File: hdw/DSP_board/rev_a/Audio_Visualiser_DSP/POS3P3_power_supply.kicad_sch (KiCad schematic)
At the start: 25 parts, among them Q401 BSS214NW, Q402 ZXMS6004FFTA, U401 74LVC1G97, U402 TPS62130A

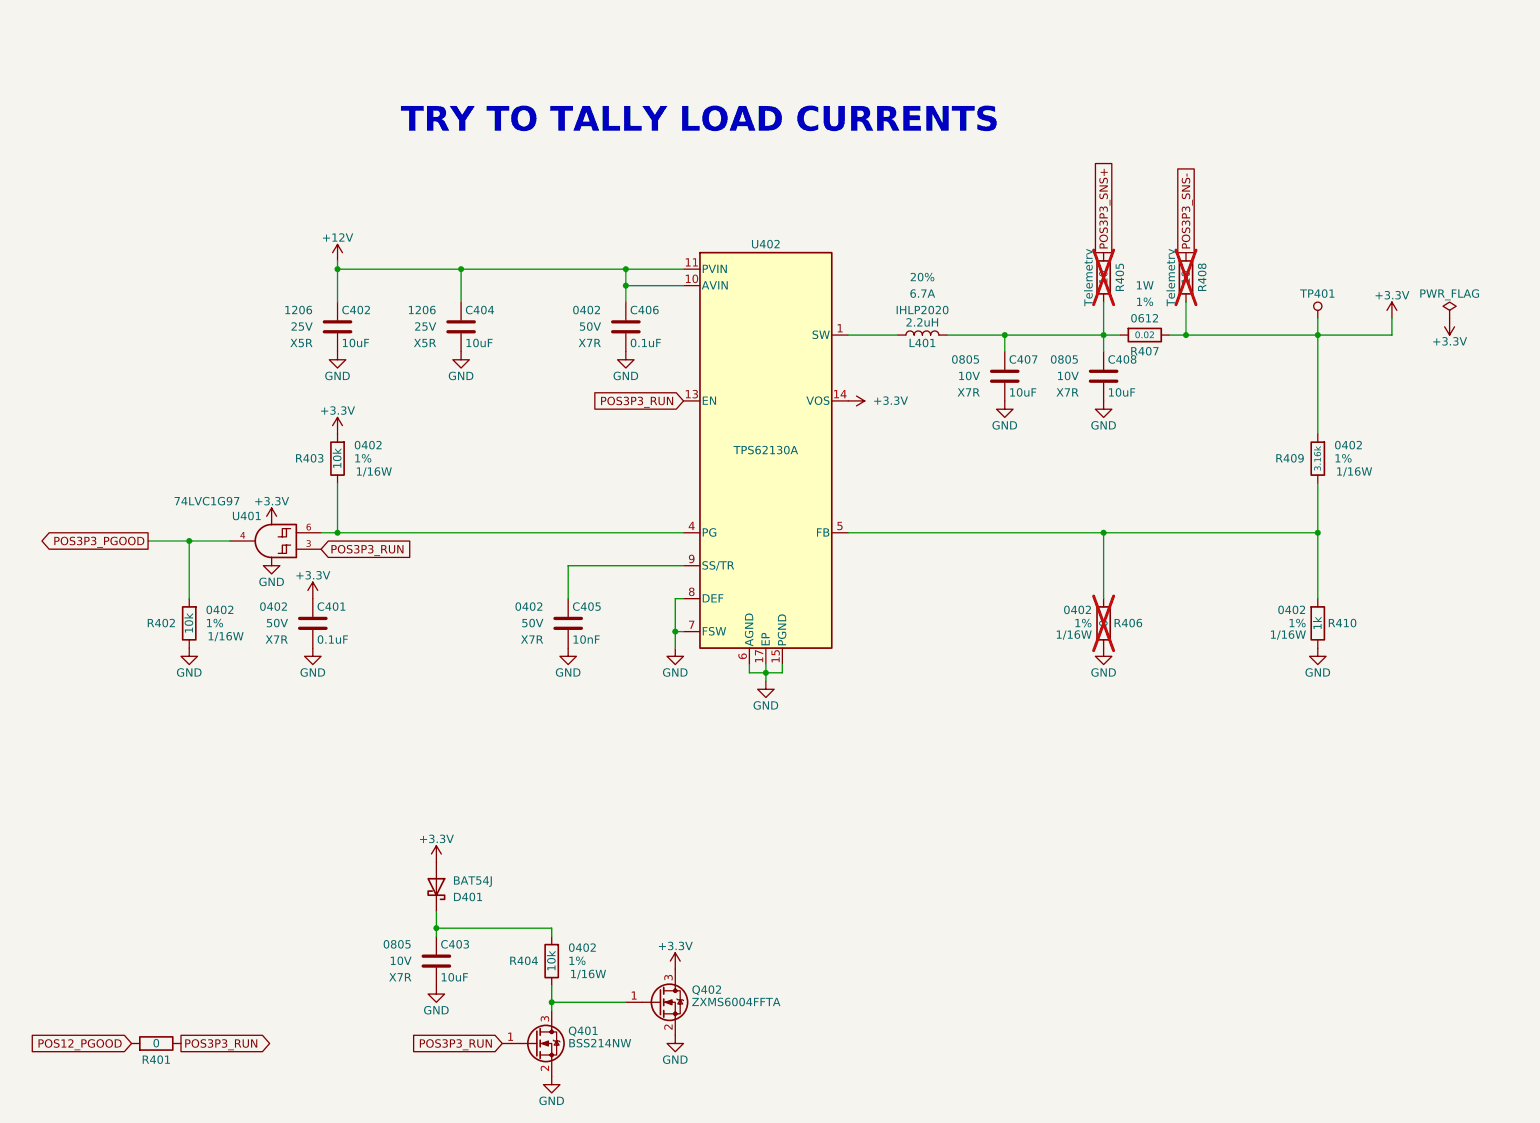
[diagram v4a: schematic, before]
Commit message: Added power draw tables
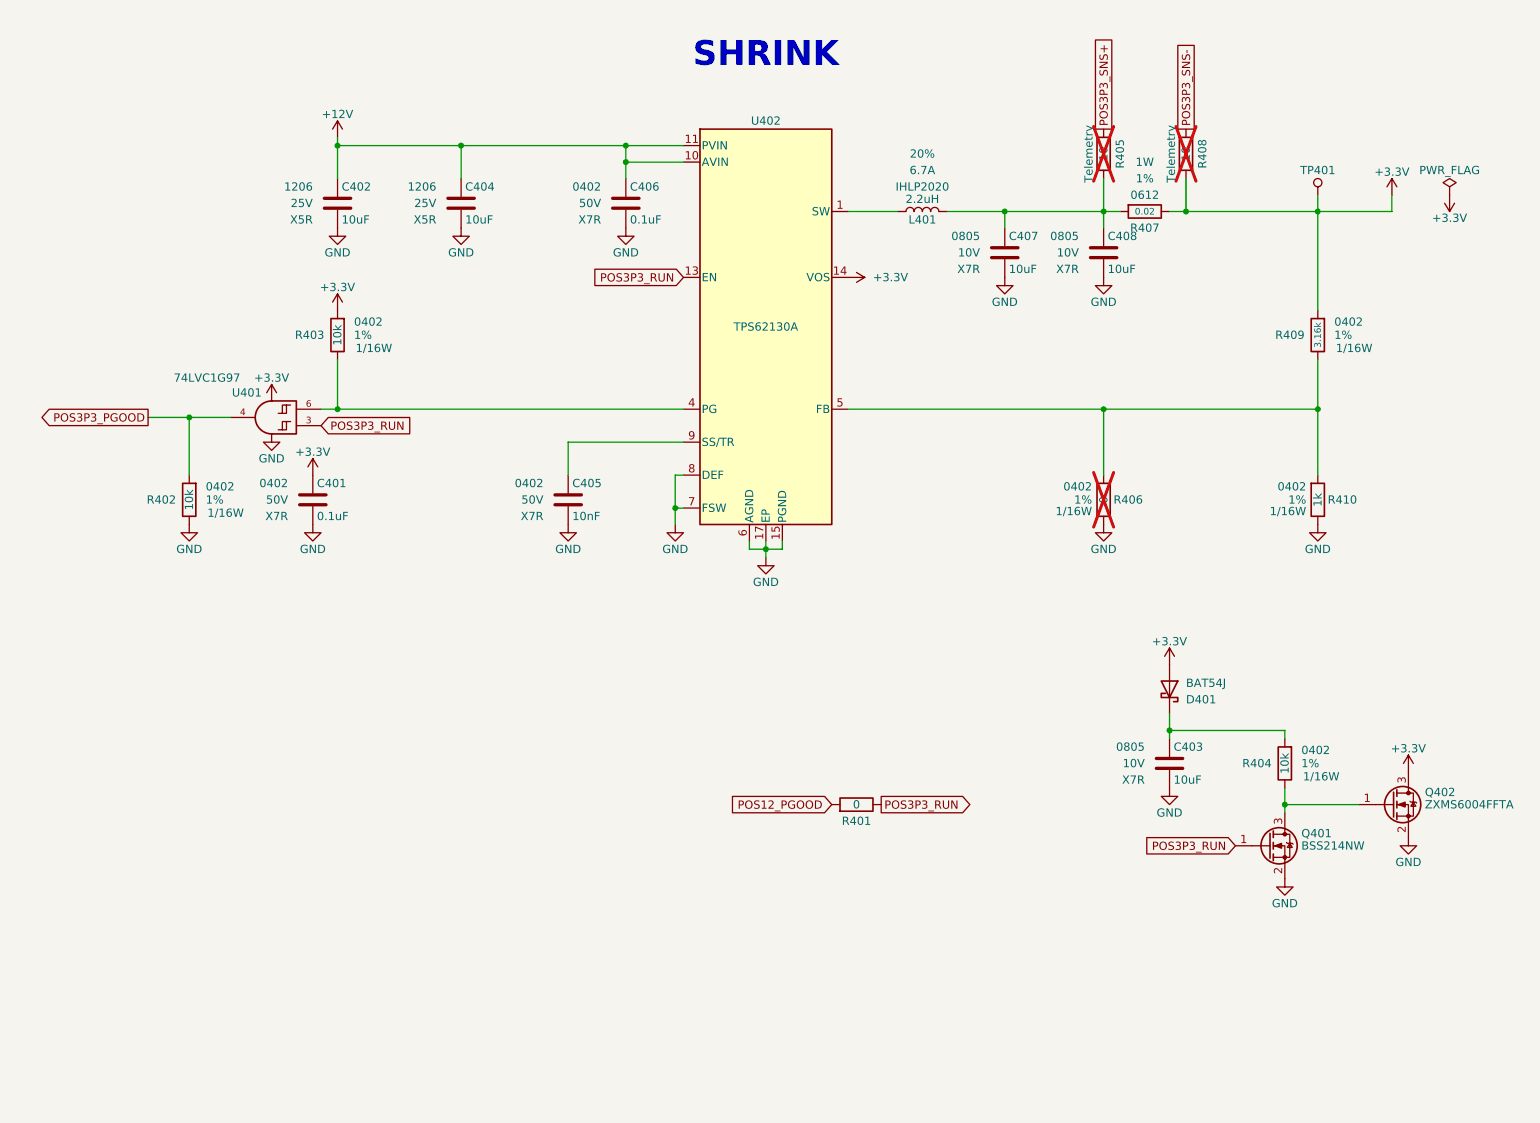
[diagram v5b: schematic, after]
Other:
- note added: "SHRINK"
- note removed: "TRY TO TALLY LOAD CURRENTS"
- moved on the sheet: C401, C402, C403, C404, C405, C406, C407, C408, D401, L401, Q401, Q402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

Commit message: Changed reference design to use op amp buffering. Changed speaker level signal divider to divide to reference voltages, not GND
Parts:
- renumbered C404 to C403, C405 to C404, C406 to C405, C407 to C406, C408 to C407, C403 to C408, R402 to R401, R403 to R402, R401 to R403, R405 to R404, R406 to R405, R407 to R406, R408 to R407, R404 to R408

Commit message: update some design notes
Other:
- note added: "Update"
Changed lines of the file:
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@@
 		(date "2023-12-25")
+	)
+	(text "Update"
+		(exclude_from_sim no)
+		(at 54.61 142.24 0)
+		(effects
+			(font
+				(size 3.81 3.81)
+				(thickness 0.762)
+				(bold yes)
+				(color 194 0 0 1)
+			)
+		)
 	)
 	(text "SHRINK"

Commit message: shrink POS3P3 Power Supply
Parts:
- L401: footprint Inductors_SMD:L_Vishay_IHLP-2020 -> Inductors_SMD:L_Vishay_IHLP-1212; Ampacity 6.7A -> 3.55A; Digi-Key PN 541-1236-1-ND -> 541-IHLP1212BZEV2R2M01CT-ND; display_footprint IHLP2020 -> IHLP1212
- U402: value TPS62130A -> TPS62150A; Digi-Key PN 296-39446-1-ND -> 296-41757-1-ND
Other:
- note removed: "SHRINK"
- note removed: "Update"
